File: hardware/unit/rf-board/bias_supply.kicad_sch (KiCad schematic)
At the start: 48 parts, among them Q1011 BC857B, Q1012 IRFL9014, Q1013 BSS138BK, Q1021 BC857B, Q1022 IRFL9014, Q1023 BSS138BK, Q1031 BC857B, Q1032 IRFL9014, Q1033 BSS138BK, Q1041 BC857B, Q1042 IRFL9014, Q1043 BSS138BK, U1001 PCA9539

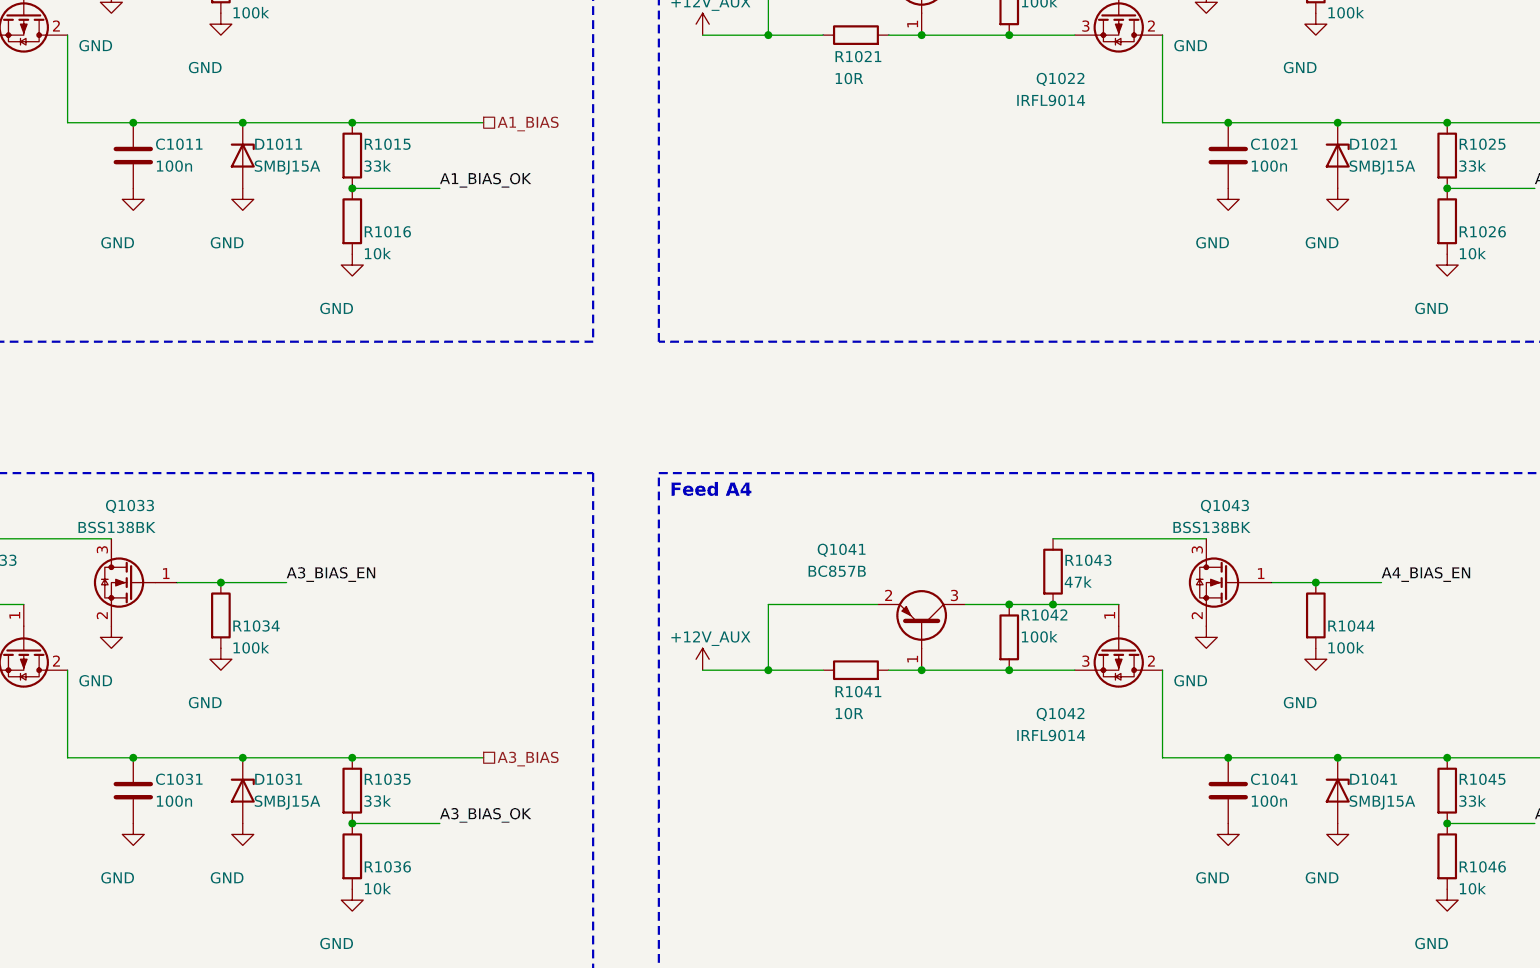
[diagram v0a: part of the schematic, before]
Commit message: Pre-order review; RF board seat keep-outs; part reuse P-1 to P-5
- docs/reviews/2026-10-31-pre-order-review.md: review of all three boards
  before ordering (verify scripts, ERC/DRC, pin maps, BOM, fab and case,
  firmware against spec, open items, part reuse).
- RF board (D-189, M-107): no other-net copper or vias under the case
  seats at S1 to S6 and the SO-239/SMA GND bosses; relay NC pads (pad 12)
  in netclass RF. Re-routed, DRC 0.
- Part reuse (D-190, M-108): one value text for 2k2, 100n 50V X7R and
  10n 50V X7R; shack PC817X order code as the controller; shack U4/U9 in
  VSSOP-8 (TI DCU, Nexperia DC) with fixed fan-out, re-routed.
  Netlists rf15, ctl15, si17; ERC 0.

Co-Authored-By: Claude Opus 5.5 <noreply@anthropic.com>
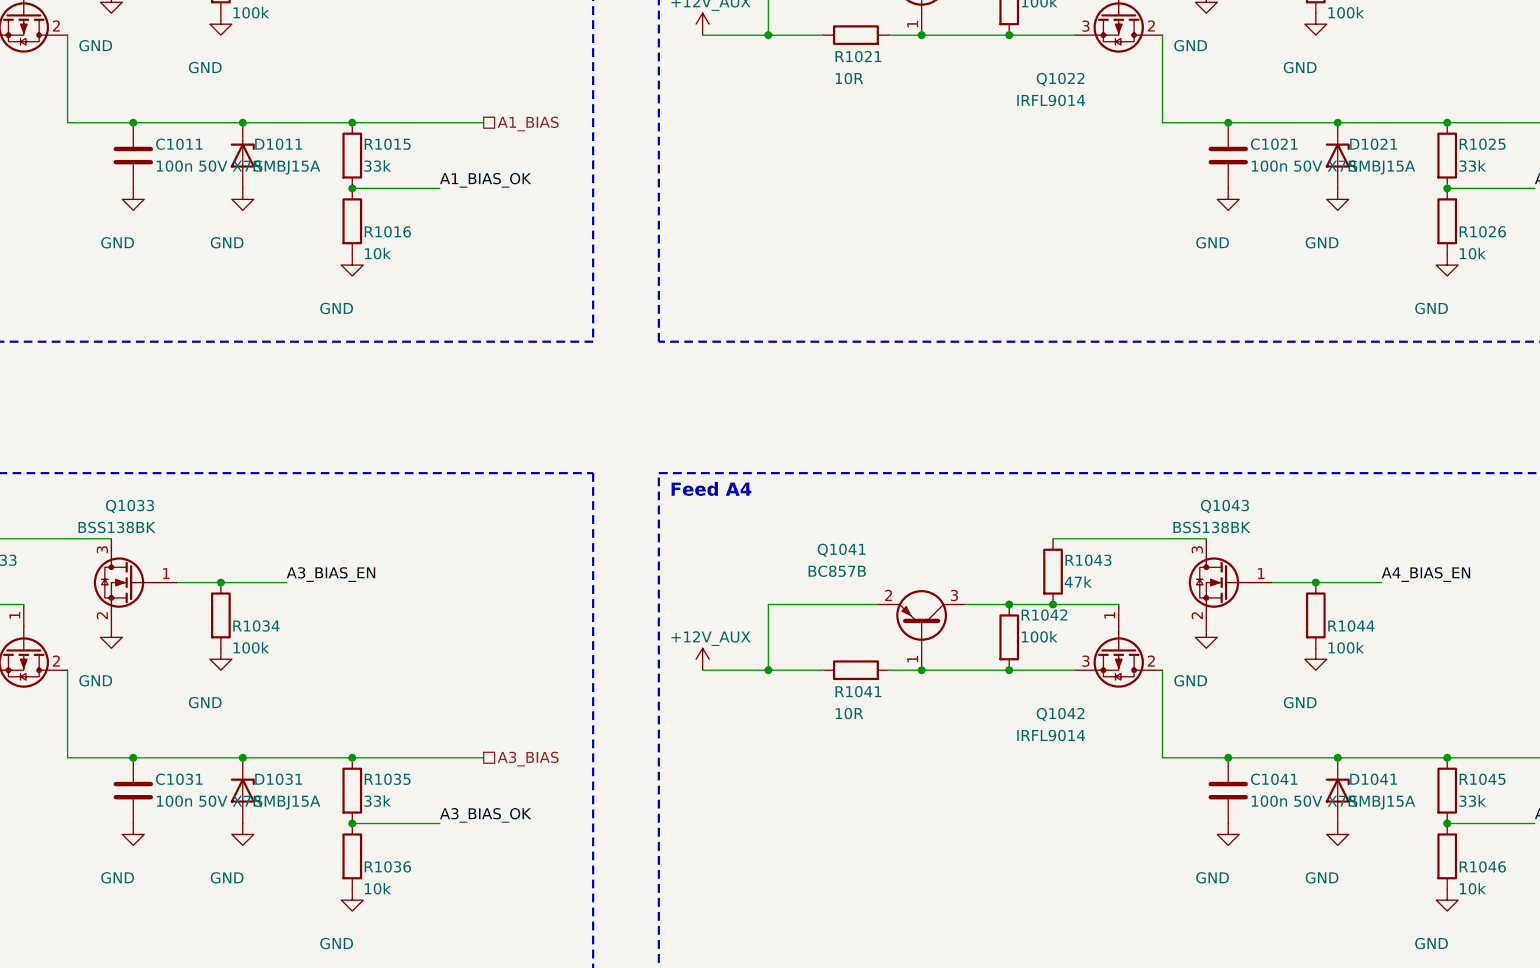
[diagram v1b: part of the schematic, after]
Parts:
- C1011, C1021, C1031, C1041: value 100n -> 100n 50V X7R
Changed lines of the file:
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@@
 			)
 		)
-		(property "Value" "100n"
+		(property "Value" "100n 50V X7R"
 			(at 215.9 83.82 0)
 			(show_name no)
@@
 			)
 		)
-		(property "Value" "100n"
+		(property "Value" "100n 50V X7R"
 			(at 342.9 83.82 0)
 			(show_name no)
@@
 			)
 		)
-		(property "Value" "100n"
+		(property "Value" "100n 50V X7R"
 			(at 215.9 157.48 0)
 			(show_name no)
@@
 			)
 		)
-		(property "Value" "100n"
+		(property "Value" "100n 50V X7R"
 			(at 342.9 157.48 0)
 			(show_name no)

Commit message: S-4: MPN BSS138BK,215 (Nexperia) on RF and shack (M-115)
The ROHM BSS138BKT116 has the same name and another pin order. All 45
BSS138BK (RF 42, shack 3) now carry MPN BSS138BK,215. Nexperia pinning
1 G, 2 S, 3 D matches the footprint. ERC 0 on both; boards and
netlists unchanged.

Co-Authored-By: Claude Opus 5.5 <noreply@anthropic.com>
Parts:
- Q1013, Q1023, Q1033, Q1043: MPN BSS138BK -> BSS138BK,215
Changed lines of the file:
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@@
 			)
 		)
-		(property "MPN" "BSS138BK"
+		(property "MPN" "BSS138BK,215"
 			(at 213.36 58.42 0)
 			(hide yes)
@@
 			)
 		)
-		(property "MPN" "BSS138BK"
+		(property "MPN" "BSS138BK,215"
 			(at 340.36 58.42 0)
 			(hide yes)
@@
 			)
 		)
-		(property "MPN" "BSS138BK"
+		(property "MPN" "BSS138BK,215"
 			(at 213.36 132.08 0)
 			(hide yes)
@@
 			)
 		)
-		(property "MPN" "BSS138BK"
+		(property "MPN" "BSS138BK,215"
 			(at 340.36 132.08 0)
 			(hide yes)

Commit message: S-10: MAX823SEUK+T first source, IRFL9014TRPBF-BE3 (D-195, M-118)
Supervisor U12 (controller), U3 and U6 (shack): MAX823SEUK+T first,
TPS3823A-33DBVR and APX823-29W5G-7 second. Same pin-out; RESET_N loads
are CMOS inputs; WDI and MR behave as the TPS3823 in our circuits.
RF Q1012 to Q1042: IRFL9014TRPBF-BE3. TLP176AM in stock at Mouser.
SO-239 83-798 stays single source, order first. Values and boards
unchanged. ERC 0 on all three.

Co-Authored-By: Claude Opus 5.5 <noreply@anthropic.com>
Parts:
- Q1012, Q1022, Q1032, Q1042: MPN IRFL9014TRPBF -> IRFL9014TRPBF-BE3
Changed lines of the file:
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@@
 			)
 		)
-		(property "MPN" "IRFL9014TRPBF"
+		(property "MPN" "IRFL9014TRPBF-BE3"
 			(at 200.66 66.04 0)
 			(hide yes)
@@
 			)
 		)
-		(property "MPN" "IRFL9014TRPBF"
+		(property "MPN" "IRFL9014TRPBF-BE3"
 			(at 327.66 66.04 0)
 			(hide yes)
@@
 			)
 		)
-		(property "MPN" "IRFL9014TRPBF"
+		(property "MPN" "IRFL9014TRPBF-BE3"
 			(at 200.66 139.7 0)
 			(hide yes)
@@
 			)
 		)
-		(property "MPN" "IRFL9014TRPBF"
+		(property "MPN" "IRFL9014TRPBF-BE3"
 			(at 327.66 139.7 0)
 			(hide yes)
